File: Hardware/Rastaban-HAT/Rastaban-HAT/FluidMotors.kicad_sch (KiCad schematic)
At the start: 8 parts, among them U3 TMC2208_SILENTSTEPSTICK, U4 TMC2208_SILENTSTEPSTICK

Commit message: cleanup and changed some names to Rastaban
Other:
- title: Water Quality Monitor -> Rastaban-HAT
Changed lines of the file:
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@@
   (paper "A4")
   (title_block
-    (title "Water Quality Monitor")
+    (title "Rastaban-HAT")
     (rev "1")
     (company "HAN")

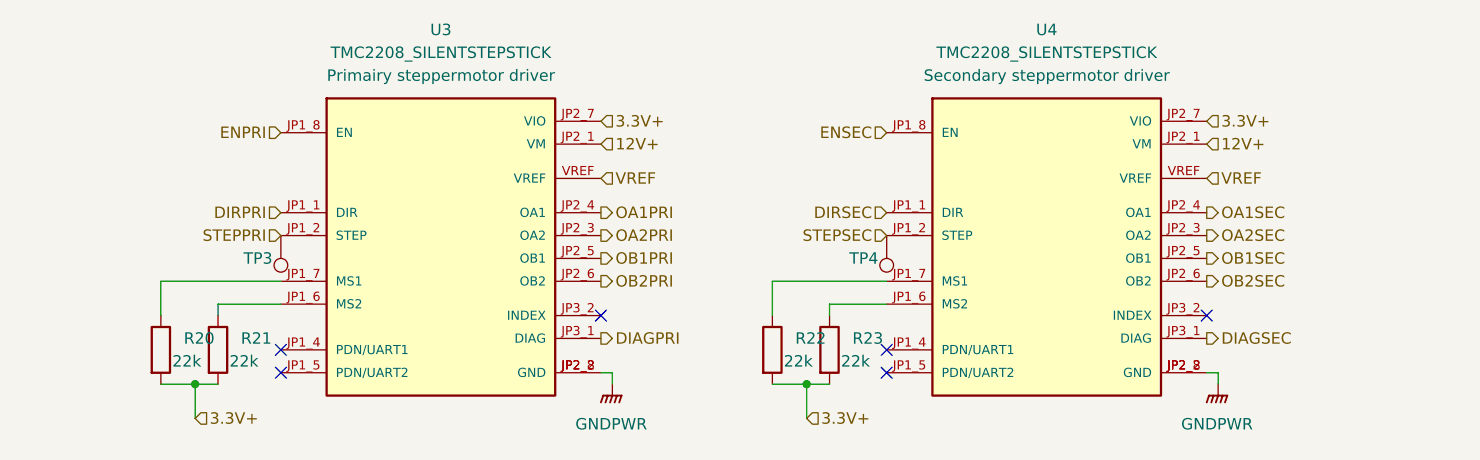
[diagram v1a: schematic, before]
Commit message: updated prim and sec stepper motor schematic
added capacitors to circuits.
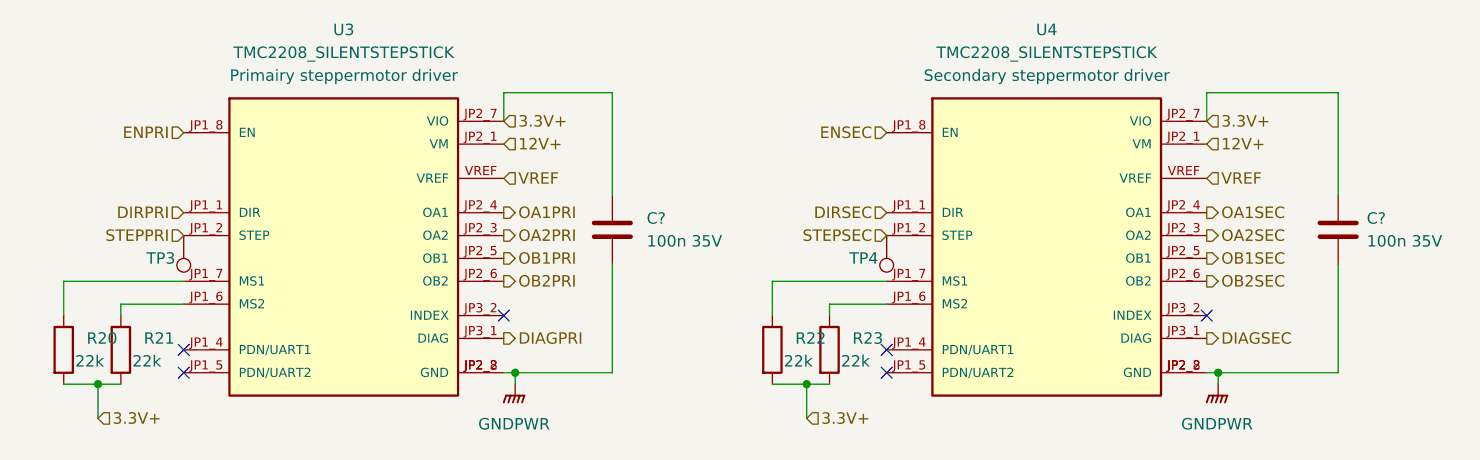
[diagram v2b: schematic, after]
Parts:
- added C? (x2): 100n 35V, symbol Device:C
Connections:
- net 3.3V+: now also C?.1, C?.1
- net GNDPWR: now also C?.2, C?.2
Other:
- moved on the sheet: R20, R21, TP3, U3

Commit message: updated all ground lables to common ground
switched back from power grounds, since they are not possible (stepper drivers)
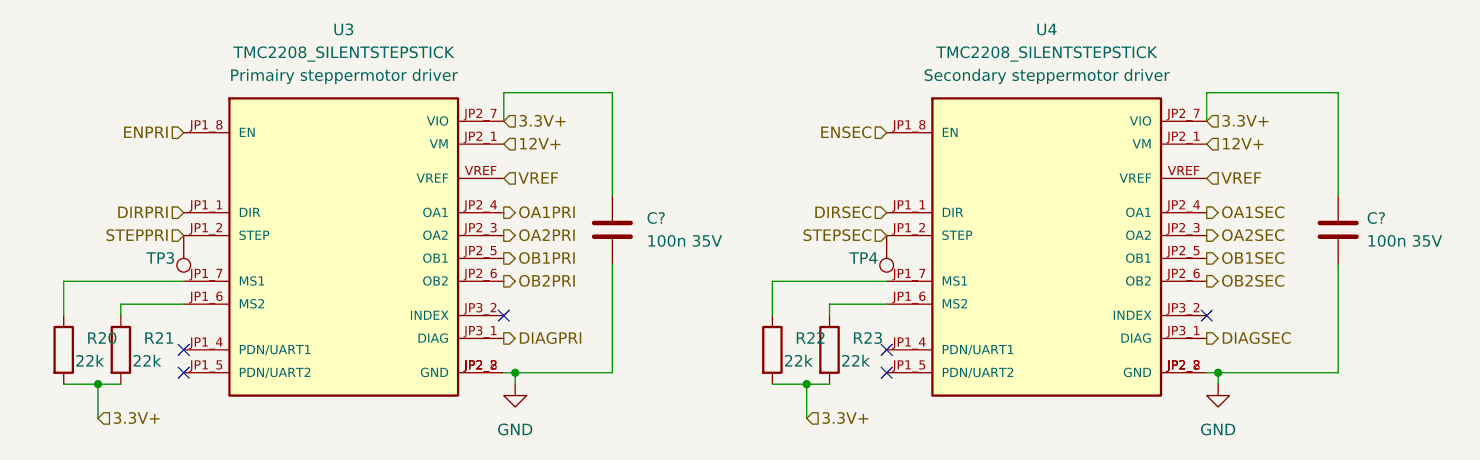
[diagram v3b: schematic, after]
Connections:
- net GNDPWR renamed GND
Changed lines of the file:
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@@
     (pin "2")
   )
-  (symbol (lib_id "power:GNDPWR") (at 203.2 118.11 0) (unit 1)
+  (symbol (lib_id "power:GND") (at 203.2 118.11 0) (unit 1)
     (in_bom yes) (on_board yes) (fields_autoplaced)
-    (property "Reference" "#PWR017" (id 0) (at 203.2 123.19 0)
+    (property "Reference" "#PWR?" (id 0) (at 203.2 124.46 0)
       (effects (font (size 1.27 1.27)) hide)
     )
-    (property "Value" "GNDPWR" (id 1) (at 203.073 122.555 0))
-    (property "Footprint" "" (id 2) (at 203.2 119.38 0)
+    (property "Value" "GND" (id 1) (at 203.2 123.19 0))
+    (property "Footprint" "" (id 2) (at 203.2 118.11 0)
       (effects (font (size 1.27 1.27)) hide)
     )
-    (property "Datasheet" "" (id 3) (at 203.2 119.38 0)
-      (effects (font (size 1.27 1.27)) hide)
-    )
-    (pin "1")
-  )
-  (symbol (lib_id "power:GNDPWR") (at 125.095 118.11 0) (unit 1)
-    (in_bom yes) (on_board yes) (fields_autoplaced)
-    (property "Reference" "#PWR016" (id 0) (at 125.095 123.19 0)
-      (effects (font (size 1.27 1.27)) hide)
-    )
-    (property "Value" "GNDPWR" (id 1) (at 124.968 122.555 0))
-    (property "Footprint" "" (id 2) (at 125.095 119.38 0)
-      (effects (font (size 1.27 1.27)) hide)
-    )
-    (property "Datasheet" "" (id 3) (at 125.095 119.38 0)
+    (property "Datasheet" "" (id 3) (at 203.2 118.11 0)
       (effects (font (size 1.27 1.27)) hide)
     )
@@
     (pin "VREF")
   )
+  (symbol (lib_id "power:GND") (at 125.095 118.11 0) (unit 1)
+    (in_bom yes) (on_board yes) (fields_autoplaced)
+    (property "Reference" "#PWR?" (id 0) (at 125.095 124.46 0)
+      (effects (font (size 1.27 1.27)) hide)
+    )
+    (property "Value" "GND" (id 1) (at 125.095 123.19 0))
+    (property "Footprint" "" (id 2) (at 125.095 118.11 0)
+      (effects (font (size 1.27 1.27)) hide)
+    )
+    (property "Datasheet" "" (id 3) (at 125.095 118.11 0)
+      (effects (font (size 1.27 1.27)) hide)
+    )
+    (pin "1")
+  )
   (symbol (lib_id "Device:R") (at 74.93 114.3 0) (unit 1)

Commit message: enh motor global labels
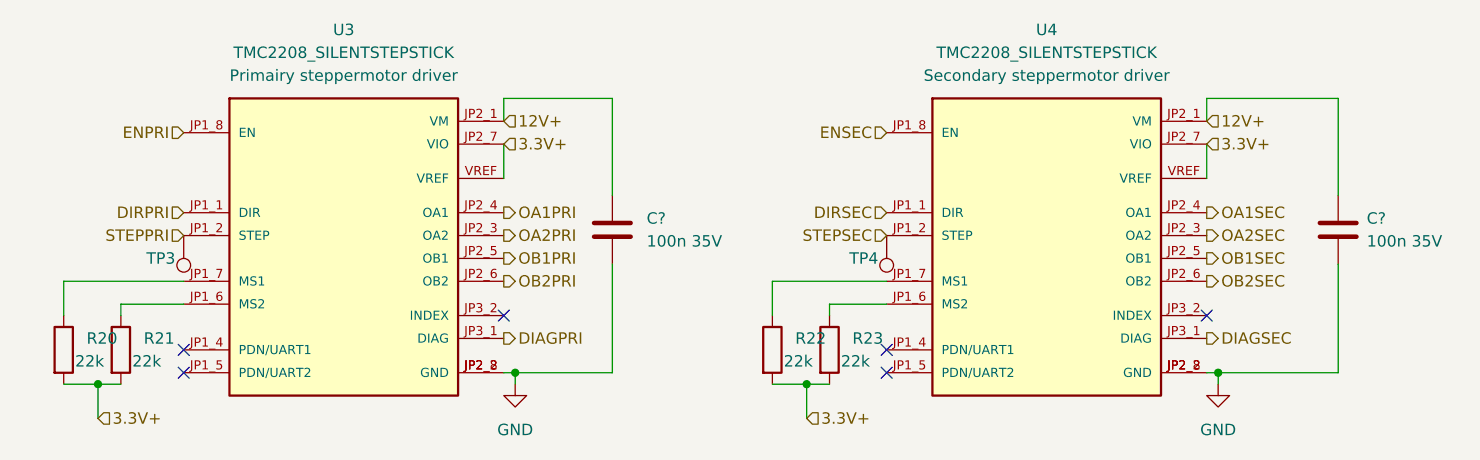
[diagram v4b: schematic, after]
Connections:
- net VREF is gone; now on net 3.3V+: U3.VREF, U4.VREF
- net 12V+: now also C?.1, C?.1
- net 3.3V+: no longer C?.1, C?.1
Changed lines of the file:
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@@
   (no_connect (at 88.265 116.84))
   (no_connect (at 166.37 116.84))
+  (wire (pts (xy 216.535 86.36) (xy 201.93 86.36))
+    (stroke (width 0) (type default) (color 0 0 0 0))
+  )
   (wire (pts (xy 203.2 116.84) (xy 201.93 116.84))
     (stroke (width 0) (type default) (color 0 0 0 0))
   )
   (wire (pts (xy 216.535 116.84) (xy 216.535 104.775))
+    (stroke (width 0) (type default) (color 0 0 0 0))
+  )
+  (wire (pts (xy 123.825 86.36) (xy 123.825 88.9))
     (stroke (width 0) (type default) (color 0 0 0 0))
   )
@@
     (stroke (width 0) (type default) (color 0 0 0 0))
   )
+  (wire (pts (xy 123.825 91.44) (xy 123.825 95.25))
+    (stroke (width 0) (type default) (color 0 0 0 0))
+  )
   (wire (pts (xy 160.02 109.22) (xy 160.02 110.49))
     (stroke (width 0) (type default) (color 0 0 0 0))
@@
     (stroke (width 0) (type default) (color 0 0 0 0))
   )
-  (wire (pts (xy 216.535 97.155) (xy 216.535 85.725))
+  (wire (pts (xy 201.93 91.44) (xy 201.93 95.25))
     (stroke (width 0) (type default) (color 0 0 0 0))
   )
-  (wire (pts (xy 201.93 85.725) (xy 201.93 88.9))
+  (wire (pts (xy 201.93 86.36) (xy 201.93 88.9))
     (stroke (width 0) (type default) (color 0 0 0 0))
   )
@@
   )
   (wire (pts (xy 160.02 109.22) (xy 166.37 109.22))
-    (stroke (width 0) (type default) (color 0 0 0 0))
-  )
-  (wire (pts (xy 123.825 88.9) (xy 123.825 85.725))
     (stroke (width 0) (type default) (color 0 0 0 0))
   )
@@
     (stroke (width 0) (type default) (color 0 0 0 0))
   )
-  (wire (pts (xy 216.535 85.725) (xy 201.93 85.725))
-    (stroke (width 0) (type default) (color 0 0 0 0))
-  )
   (wire (pts (xy 203.2 118.11) (xy 203.2 116.84))
     (stroke (width 0) (type default) (color 0 0 0 0))
   )
-  (wire (pts (xy 123.825 85.725) (xy 135.89 85.725))
+  (wire (pts (xy 135.89 86.36) (xy 123.825 86.36))
+    (stroke (width 0) (type default) (color 0 0 0 0))
+  )
+  (wire (pts (xy 216.535 86.36) (xy 216.535 97.155))
     (stroke (width 0) (type default) (color 0 0 0 0))
   )
   (wire (pts (xy 157.48 118.11) (xy 160.02 118.11))
-    (stroke (width 0) (type default) (color 0 0 0 0))
-  )
-  (wire (pts (xy 135.89 85.725) (xy 135.89 97.155))
     (stroke (width 0) (type default) (color 0 0 0 0))
   )
@@
   )
   (wire (pts (xy 135.89 104.775) (xy 135.89 116.84))
+    (stroke (width 0) (type default) (color 0 0 0 0))
+  )
+  (wire (pts (xy 135.89 86.36) (xy 135.89 97.155))
     (stroke (width 0) (type default) (color 0 0 0 0))
   )
@@
     (effects (font (size 1.27 1.27)) (justify left))
   )
-  (hierarchical_label "VREF" (shape input) (at 201.93 95.25 0)
-    (effects (font (size 1.27 1.27)) (justify left))
-  )
   (hierarchical_label "DIAGPRI" (shape output) (at 123.825 113.03 0)
     (effects (font (size 1.27 1.27)) (justify left))
   )
-  (hierarchical_label "3.3V+" (shape input) (at 123.825 88.9 0)
+  (hierarchical_label "3.3V+" (shape input) (at 123.825 91.44 0)
     (effects (font (size 1.27 1.27)) (justify left))
   )
@@
     (effects (font (size 1.27 1.27)) (justify right))
   )
-  (hierarchical_label "VREF" (shape input) (at 123.825 95.25 0)
-    (effects (font (size 1.27 1.27)) (justify left))
-  )
   (hierarchical_label "OA2PRI" (shape output) (at 123.825 101.6 0)
     (effects (font (size 1.27 1.27)) (justify left))
   )
-  (hierarchical_label "12V+" (shape input) (at 123.825 91.44 0)
+  (hierarchical_label "12V+" (shape input) (at 123.825 88.9 0)
     (effects (font (size 1.27 1.27)) (justify left))
   )
@@
     (effects (font (size 1.27 1.27)) (justify left))
   )
-  (hierarchical_label "3.3V+" (shape input) (at 201.93 88.9 0)
+  (hierarchical_label "3.3V+" (shape input) (at 201.93 91.44 0)
     (effects (font (size 1.27 1.27)) (justify left))
   )
-  (hierarchical_label "12V+" (shape input) (at 201.93 91.44 0)
+  (hierarchical_label "12V+" (shape input) (at 201.93 88.9 0)
     (effects (font (size 1.27 1.27)) (justify left))
   )
@@
     (pin "1")
   )
-  (symbol (lib_name "TMC2208_SILENTSTEPSTICK_1") (lib_id "TMC2208_SILENTSTEPSTICK:TMC2208_SILENTSTEPSTICK") (at 184.15 104.14 0) (unit 1)
+  (symbol (lib_name "TMC2208_SILENTSTEPSTICK_2") (lib_id "TMC2208_SILENTSTEPSTICK:TMC2208_SILENTSTEPSTICK") (at 184.15 104.14 0) (unit 1)
     (in_bom yes) (on_board yes)
     (property "Reference" "U4" (id 0) (at 184.15 78.74 0))

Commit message: added new POLOLU DRV8838 schematic and enh main
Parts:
- gave numbers to parts that had none: 2
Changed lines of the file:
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@@
   (symbol (lib_id "power:GND") (at 203.2 118.11 0) (unit 1)
     (in_bom yes) (on_board yes) (fields_autoplaced)
-    (property "Reference" "#PWR?" (id 0) (at 203.2 124.46 0)
+    (property "Reference" "#PWR016" (id 0) (at 203.2 124.46 0)
       (effects (font (size 1.27 1.27)) hide)
     )
@@
   (symbol (lib_id "Device:C") (at 135.89 100.965 0) (unit 1)
     (in_bom yes) (on_board yes) (fields_autoplaced)
-    (property "Reference" "C?" (id 0) (at 139.7 99.6949 0)
+    (property "Reference" "C16" (id 0) (at 139.7 99.6949 0)
       (effects (font (size 1.27 1.27)) (justify left))
     )
@@
   (symbol (lib_id "power:GND") (at 125.095 118.11 0) (unit 1)
     (in_bom yes) (on_board yes) (fields_autoplaced)
-    (property "Reference" "#PWR?" (id 0) (at 125.095 124.46 0)
+    (property "Reference" "#PWR015" (id 0) (at 125.095 124.46 0)
       (effects (font (size 1.27 1.27)) hide)
     )
@@
   (symbol (lib_id "Device:C") (at 216.535 100.965 0) (unit 1)
     (in_bom yes) (on_board yes) (fields_autoplaced)
-    (property "Reference" "C?" (id 0) (at 219.71 99.6949 0)
+    (property "Reference" "C17" (id 0) (at 219.71 99.6949 0)
       (effects (font (size 1.27 1.27)) (justify left))
     )

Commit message: updated some names on symbols
stepper motor drivers
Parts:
- U3, U4: value TMC2208_SILENTSTEPSTICK -> TMC2208_Carrier
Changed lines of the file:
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@@
     (in_bom yes) (on_board yes)
     (property "Reference" "U4" (id 0) (at 184.15 78.74 0))
-    (property "Value" "TMC2208_SILENTSTEPSTICK" (id 1) (at 184.15 81.28 0))
+    (property "Value" "TMC2208_Carrier" (id 1) (at 184.15 81.28 0))
     (property "Footprint" "Footprints:TMC2208_SILENTSTEPSTICK" (id 2) (at 168.91 123.19 0)
       (effects (font (size 1.27 1.27)) (justify left bottom) hide)
@@
     (in_bom yes) (on_board yes) (fields_autoplaced)
     (property "Reference" "U3" (id 0) (at 106.045 78.74 0))
-    (property "Value" "TMC2208_SILENTSTEPSTICK" (id 1) (at 106.045 81.28 0))
+    (property "Value" "TMC2208_Carrier" (id 1) (at 106.045 81.28 0))
     (property "Footprint" "Footprints:TMC2208_SILENTSTEPSTICK" (id 2) (at 90.805 123.19 0)
       (effects (font (size 1.27 1.27)) (justify left bottom) hide)

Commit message: changed revision to v1.1 on all tabs
changed some capacitor values
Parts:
- C16, C17: value 100n 35V -> 100u 35V
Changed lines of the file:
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@@
   (title_block
     (title "Rastaban-HAT")
-    (rev "1")
+    (rev "1.1")
     (company "HAN")
     (comment 1 "Casper R. Tak")
@@
       (effects (font (size 1.27 1.27)) (justify left))
     )
-    (property "Value" "100n 35V" (id 1) (at 139.7 102.2349 0)
+    (property "Value" "100u 35V" (id 1) (at 139.7 102.2349 0)
       (effects (font (size 1.27 1.27)) (justify left))
     )
@@
       (effects (font (size 1.27 1.27)) (justify left))
     )
-    (property "Value" "100n 35V" (id 1) (at 219.71 102.2349 0)
-      (effects (font (size 1.27 1.27)) (justify left))
-    )
+    (property "Value" "100u 35V" (id 1) (at 219.71 102.2349 0)
+      (effects (font (size 1.27 1.27)) (justify left))
+    )

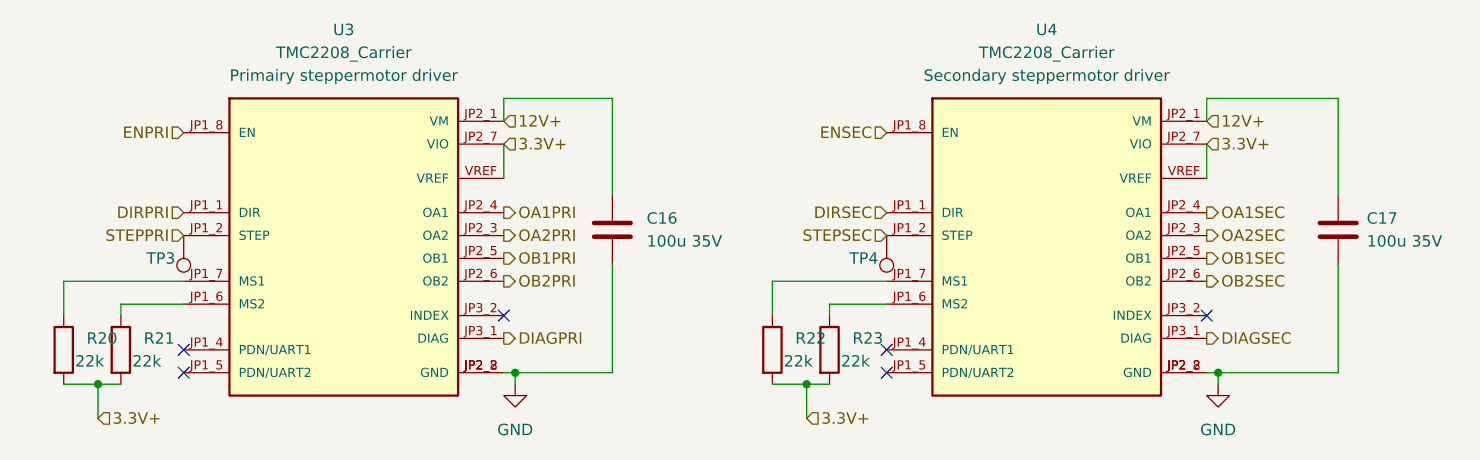
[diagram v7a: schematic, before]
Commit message: Heavily improved symbol text placements
all texts are now readable
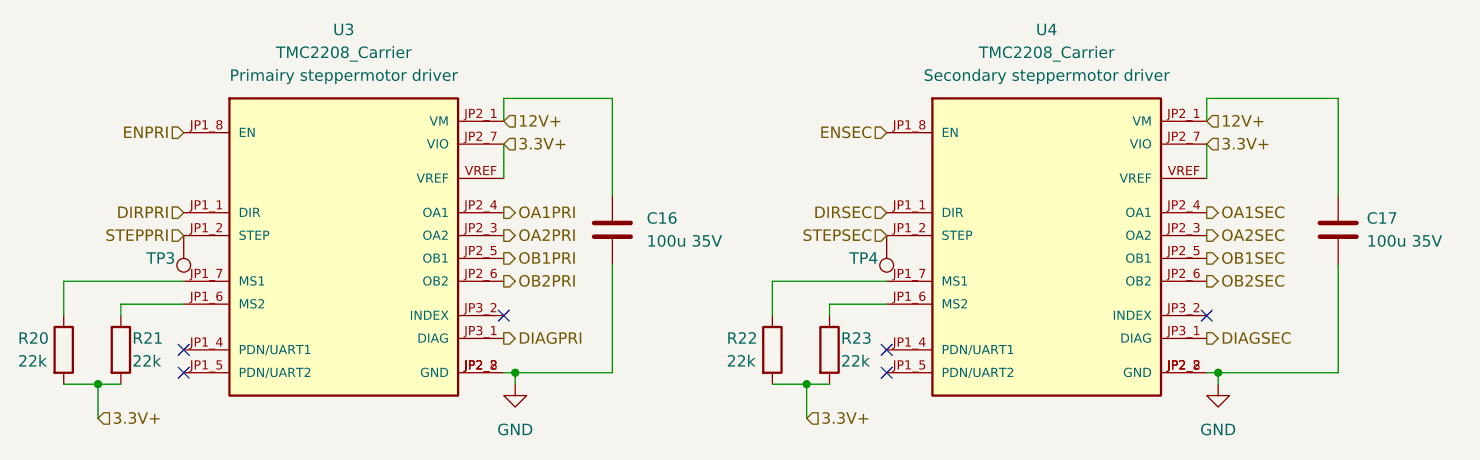
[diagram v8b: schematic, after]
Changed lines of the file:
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@@
   (symbol (lib_id "Device:R") (at 153.67 114.3 0) (unit 1)
     (in_bom yes) (on_board yes)
-    (property "Reference" "R22" (id 0) (at 156.21 113.0299 0)
+    (property "Reference" "R22" (id 0) (at 148.59 113.03 0)
       (effects (font (size 1.27 1.27)) (justify left))
     )
-    (property "Value" "22k" (id 1) (at 154.94 115.57 0)
+    (property "Value" "22k" (id 1) (at 148.59 115.57 0)
       (effects (font (size 1.27 1.27)) (justify left))
     )
@@
   (symbol (lib_id "Device:R") (at 81.28 114.3 0) (unit 1)
     (in_bom yes) (on_board yes)
-    (property "Reference" "R21" (id 0) (at 83.82 113.0299 0)
+    (property "Reference" "R21" (id 0) (at 82.55 113.03 0)
       (effects (font (size 1.27 1.27)) (justify left))
     )
@@
   (symbol (lib_id "Device:R") (at 160.02 114.3 0) (unit 1)
     (in_bom yes) (on_board yes)
-    (property "Reference" "R23" (id 0) (at 162.56 113.0299 0)
+    (property "Reference" "R23" (id 0) (at 161.29 113.03 0)
       (effects (font (size 1.27 1.27)) (justify left))
     )
@@
   (symbol (lib_id "Device:R") (at 74.93 114.3 0) (unit 1)
     (in_bom yes) (on_board yes)
-    (property "Reference" "R20" (id 0) (at 77.47 113.0299 0)
+    (property "Reference" "R20" (id 0) (at 69.85 113.03 0)
       (effects (font (size 1.27 1.27)) (justify left))
     )
-    (property "Value" "22k" (id 1) (at 76.2 115.57 0)
+    (property "Value" "22k" (id 1) (at 69.85 115.57 0)
       (effects (font (size 1.27 1.27)) (justify left))
     )
